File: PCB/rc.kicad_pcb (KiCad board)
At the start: 2 copper layers, 54.9 x 25.4 mm, 8 parts, among them J1 USB_C_Receptacle_USB2.0_16P, J2 USB_A, J3 OLED display, U1 ESP32-S3-WROOM-1U, U2 MAX3421EEHJ+T, U3 ME6211C33M5

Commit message: pcb update
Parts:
- added C3: C, Capacitor_SMD:C_0402_1005Metric_Pad0.74x0.62mm_HandSolder, B.Cu at (40.1, 69.1)
- added C4: C, Capacitor_SMD:C_0402_1005Metric_Pad0.74x0.62mm_HandSolder, B.Cu at (44.2, 71.9)
- added C5: C, Capacitor_SMD:C_0402_1005Metric_Pad0.74x0.62mm_HandSolder, B.Cu at (57.4, 63.2)
- added C7: C, Capacitor_SMD:C_0402_1005Metric_Pad0.74x0.62mm_HandSolder, B.Cu at (46.5, 71.4)
- added D1: ESD9B5.0ST5G, Diode_SMD:D_SOD-923, B.Cu at (48.0, 68.5)
- added D2: ESD9B5.0ST5G, Diode_SMD:D_SOD-923, B.Cu at (49.0, 68.5)
- added FB1: FerriteBead, Inductor_SMD:L_0603_1608Metric, B.Cu at (48.5, 70.8)
- added FB2: FerriteBead, Inductor_SMD:L_0603_1608Metric, B.Cu at (61.7, 66.0)
- added R1: R_US, Resistor_SMD:R_0402_1005Metric_Pad0.72x0.64mm_HandSolder, B.Cu at (50.0, 69.5)
- added R2: R_US, Resistor_SMD:R_0402_1005Metric_Pad0.72x0.64mm_HandSolder, B.Cu at (47.0, 69.1)
- added R3: R_US, Resistor_SMD:R_0402_1005Metric_Pad0.72x0.64mm_HandSolder, B.Cu at (50.5, 72.4)
- added REF**: MountingHole_2.2mm_M2_ISO7380_Pad_TopBottom, MountingHole:MountingHole_2.2mm_M2_ISO7380_Pad_TopBottom, F.Cu at (73.7, 53.3)
- added REF**: MountingHole_2.2mm_M2_ISO7380_Pad_TopBottom, MountingHole:MountingHole_2.2mm_M2_ISO7380_Pad_TopBottom, F.Cu at (31.1, 73.7)
- added REF**: MountingHole_2.2mm_M2_ISO7380_Pad_TopBottom, MountingHole:MountingHole_2.2mm_M2_ISO7380_Pad_TopBottom, F.Cu at (31.1, 53.3)
- added REF**: MountingHole_2.2mm_M2_ISO7380_Pad_TopBottom, MountingHole:MountingHole_2.2mm_M2_ISO7380_Pad_TopBottom, F.Cu at (73.7, 73.7)
- added Y1: Crystal, Crystal:Crystal_SMD_G8-2Pin_3.2x1.5mm, B.Cu at (42.7, 70.1)
- C1, C2, J1, U2, U3: moved to B.Cu
- J3: footprint Connector_PinSocket_1.27mm:PinSocket_1x07_P1.27mm_Vertical -> Connector_PinSocket_2.54mm:PinSocket_1x07_P2.54mm_Horizontal
- moved U2 24.8 mm to (47.2, 62.0), turned to -90 degrees
- moved C2 24.3 mm to (37.1, 65.4), turned to -90 degrees
- moved C1 22.5 mm to (39.0, 65.4), turned to -90 degrees
- moved U3 20.1 mm to (37.4, 61.2), turned to -90 degrees
- moved J3 11.4 mm to (44.7, 53.1), turned to 90 degrees
- moved J2 9.91 mm to (59.7, 63.1)
- moved J1 6.12 mm to (62.7, 72.7), turned to 180 degrees
- moved U1 4.90 mm to (43.7, 65.2)
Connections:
- C1 pad 1: Net-(J2-VBUS) -> Net-(U3-CE)
- J1 pad A4: Net-(J2-VBUS) -> Net-(U3-CE)
- J1 pad A9: Net-(J2-VBUS) -> Net-(U3-CE)
- J1 pad B4: Net-(J2-VBUS) -> Net-(U3-CE)
- J1 pad B9: Net-(J2-VBUS) -> Net-(U3-CE)
- J2 pad 2: unconnected-(J2-D--Pad2) -> Net-(J2-D-)
- J2 pad 3: unconnected-(J2-D+-Pad3) -> Net-(J2-D+)
- U1 pad 17: unconnected-(U1-IO9-Pad17) -> Net-(U1-IO9)
- U1 pad 3: unconnected-(U1-EN-Pad3) -> Net-(J3-Pin_2)
- U2 pad 18: unconnected-(U2-INT-Pad18) -> Net-(U1-IO9)
- U2 pad 2: unconnected-(U2-VL-Pad2) -> Net-(J3-Pin_2)
- U2 pad 20: unconnected-(U2-D--Pad20) -> Net-(D2-A1)
- U2 pad 21: unconnected-(U2-D+-Pad21) -> Net-(D1-A1)
- U2 pad 22: unconnected-(U2-VBCOMP-Pad22) -> Net-(U2-VBCOMP)
- U2 pad 24: unconnected-(U2-XI-Pad24) -> Net-(U2-XI)
- U2 pad 25: unconnected-(U2-XO-Pad25) -> Net-(U2-XO)
- U3 pad 1: Net-(J2-VBUS) -> Net-(U3-CE)
- U3 pad 3: Net-(J2-VBUS) -> Net-(U3-CE)
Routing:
- net Net-(U3-CE): track 0.00 -> 60.4 mm
- net Net-(U1-IO13): track 42.2 -> 5.86 mm, vias 0 -> 1
- net Net-(U1-IO10): track 46.3 -> 10.5 mm, vias 0 -> 1
- net Net-(J2-VBUS): track 34.6 -> 5.20 mm
- net Net-(J3-Pin_3): track 48.6 -> 19.5 mm, vias 0 -> 1
- net Net-(J2-D+): track 0.00 -> 25.6 mm
- net Net-(J2-D-): track 0.00 -> 18.9 mm
- net Net-(J3-Pin_6): track 27.6 -> 44.8 mm, vias 1 -> 0
- net Net-(J3-Pin_4): track 34.2 -> 17.3 mm
- net Net-(J1-SHIELD): track 34.9 -> 20.2 mm, vias 0 -> 6
- net Net-(U1-IO9): track 0.00 -> 11.5 mm, vias 0 -> 2
- net Net-(U2-XO): track 0.00 -> 10.5 mm
- net Net-(J3-Pin_5): track 20.7 -> 11.3 mm, vias 1 -> 0
- net Net-(U2-XI): track 0.00 -> 7.12 mm
- net Net-(J3-Pin_2): track 55.0 -> 49.1 mm, vias 2 -> 1
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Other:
- board size 54.9 x 25.4 mm -> 47.6 x 25.4 mm

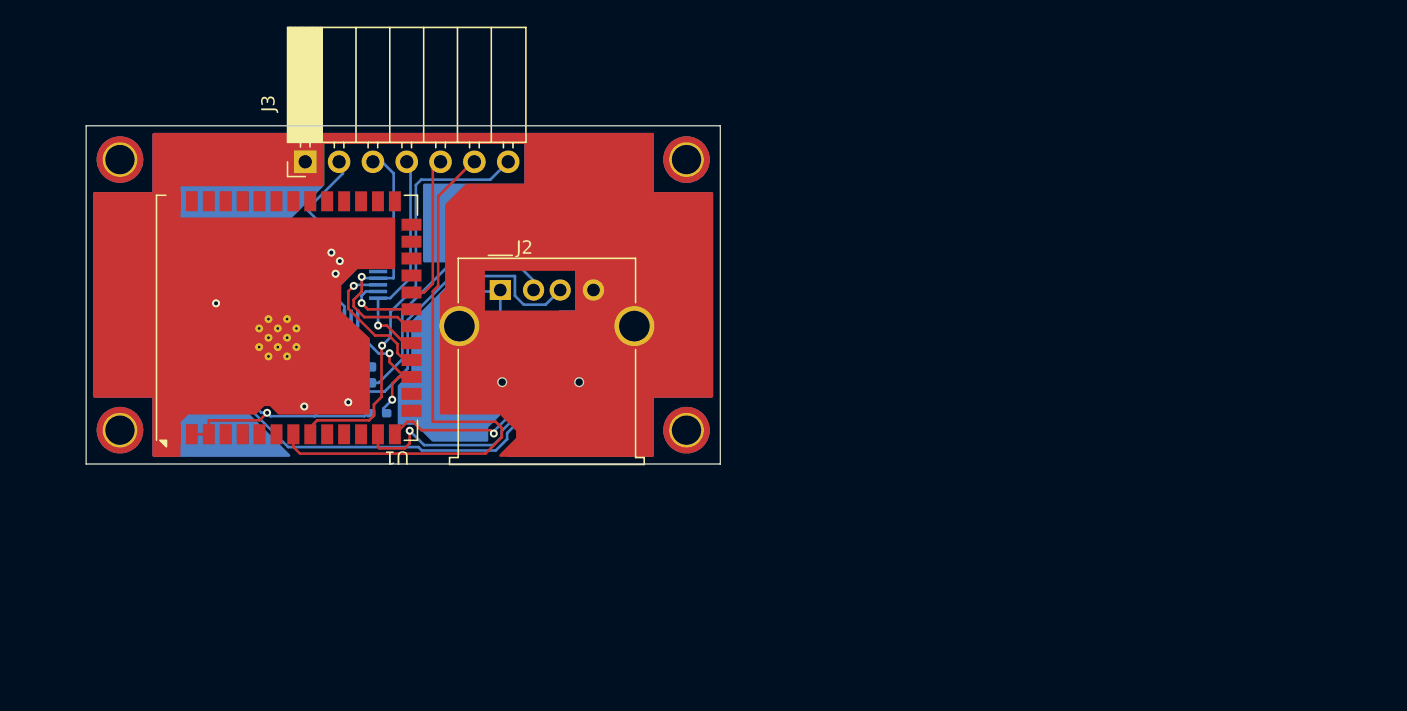
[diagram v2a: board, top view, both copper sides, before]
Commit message: 3 inch display
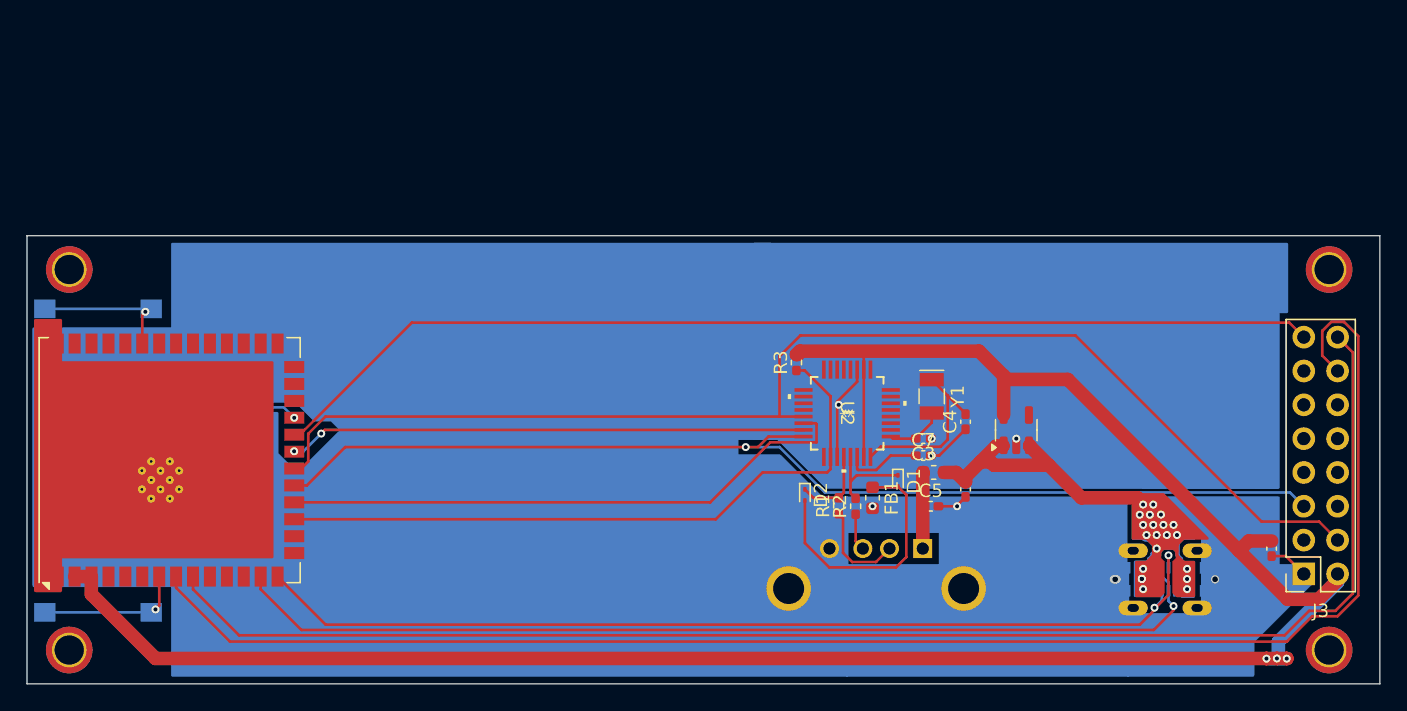
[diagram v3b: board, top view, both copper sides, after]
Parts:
- added SW1: SW_Omron_B3FS, Button_Switch_SMD:SW_SPST_Omron_B3FS-105xP, B.Cu at (29.5, 66.8)
- added SW2: SW_Omron_B3FS, Button_Switch_SMD:SW_SPST_Omron_B3FS-105xP, B.Cu at (29.5, 85.1)
- added SW3: SW_Omron_B3FS, Button_Switch_SMD:SW_SPST_Omron_B3FS-105xP, B.Cu at (29.2, 75.9)
- C1, C2, C3, C4, C5, C7, D1, D2, FB1, FB2, R1, R2, R3, U2, U3, Y1: moved to F.Cu
- J1: footprint Connector_USB:USB_C_Receptacle_GCT_USB4110 -> usbc:GCT_USB4120-03-C_REVA
- J2: footprint Connector_USB:USB_A_Molex_67643_Horizontal -> usb-a vertical:ONSHORE_USB-A1VSB6; moved to B.Cu
- J3: value OLED display -> Conn_02x08_Odd_Even; footprint Connector_PinSocket_2.54mm:PinSocket_1x07_P2.54mm_Horizontal -> Connector_PinSocket_2.54mm:PinSocket_2x08_P2.54mm_Vertical
- moved C2 82.3 mm to (117.6, 82.5)
- moved J3 81.6 mm to (120.0, 84.5), turned to 180 degrees
- moved U3 62.3 mm to (98.4, 73.7), turned to 90 degrees
- moved C1 57.1 mm to (94.6, 78.1)
- moved C3 51.6 mm to (91.4, 74.3), turned to 180 degrees
- moved REF** 51.0 mm to (121.9, 90.2)
- moved C4 50.4 mm to (94.6, 73.0), turned to 90 degrees
- moved Y1 49.4 mm to (92.1, 71.1), turned to -90 degrees
- moved REF** 49.0 mm to (121.9, 61.6)
- moved J1 48.5 mm to (109.6, 84.9)
- moved C7 45.2 mm to (91.4, 75.6), turned to 0 degrees
- moved D1 42.5 mm to (89.5, 77.5)
- moved R2 40.7 mm to (86.4, 79.4)
- moved FB1 39.9 mm to (87.6, 78.7)
- moved U2 39.9 mm to (85.7, 72.4)
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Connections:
- C1 pad 2: Net-(J1-SHIELD) -> /GND
- C2 pad 2: Net-(J1-SHIELD) -> /GND
- C3 pad 1: Net-(J1-SHIELD) -> /GND
- C4 pad 1: Net-(J1-SHIELD) -> /GND
- C5 pad 2: Net-(J1-SHIELD) -> /GND
- C7 pad 2: Net-(J1-SHIELD) -> /GND
- FB1 pad 2: Net-(J1-SHIELD) -> /GND
- J1 pad A1: Net-(J1-SHIELD) -> /GND
- J1 pad A12: Net-(J1-SHIELD) -> /GND
- J1 pad B1: Net-(J1-SHIELD) -> /GND
- J1 pad B12: Net-(J1-SHIELD) -> /GND
- J1 pad S1: Net-(J1-SHIELD) -> /GND
- J2 pad 4: Net-(J1-SHIELD) -> /GND
- J3 pad 1: Net-(J1-SHIELD) -> /GND
- J3 pad 3: Net-(J3-Pin_3) -> unconnected-(J3-Pin_3-Pad3)
- J3 pad 4: Net-(J3-Pin_4) -> /CLK
- J3 pad 5: Net-(J3-Pin_5) -> /MOSI
- J3 pad 6: Net-(J3-Pin_6) -> unconnected-(J3-Pin_6-Pad6)
- J3 pad 7: Net-(J3-Pin_7) -> unconnected-(J3-Pin_7-Pad7)
- U1 pad 1: Net-(J1-SHIELD) -> /GND
- U1 pad 19: Net-(J3-Pin_4) -> /MOSI
- U1 pad 20: Net-(J3-Pin_3) -> /CLK
- U1 pad 22: Net-(J3-Pin_5) -> /RES
- U1 pad 23: unconnected-(U1-IO21-Pad23) -> Net-(U1-IO21)
- U1 pad 35: unconnected-(U1-IO42-Pad35) -> Net-(U1-IO42)
- U1 pad 40: Net-(J1-SHIELD) -> /GND
- U1 pad 41: Net-(J1-SHIELD) -> /GND
- U1 pad 7: unconnected-(U1-IO7-Pad7) -> Net-(U1-IO7)
- U1 pad 8: Net-(J3-Pin_6) -> /DC
- U1 pad 9: Net-(J3-Pin_7) -> /CS
- U2 pad 13: Net-(J3-Pin_3) -> /CLK
- U2 pad 16: Net-(J3-Pin_4) -> /MOSI
- U2 pad 19: Net-(J1-SHIELD) -> /GND
- U2 pad 3: Net-(J1-SHIELD) -> /GND
- U3 pad 2: Net-(J1-SHIELD) -> /GND
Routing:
- net /GND: track 0.00 -> 131.6 mm, vias 0 -> 6
- net /DC: track 0.00 -> 119.1 mm
- net Net-(J3-Pin_2): track 49.1 -> 168.2 mm, vias 1 -> 3
- net /CS: track 0.00 -> 110.5 mm
- net /CLK: track 0.00 -> 94.5 mm
- net /MOSI: track 0.00 -> 83.5 mm, vias 0 -> 1
- net /RES: track 0.00 -> 79.8 mm
- net Net-(U1-IO20): track 16.7 -> 74.8 mm, vias 1 -> 2
- net Net-(U1-IO19): track 20.8 -> 74.9 mm
- net Net-(J3-Pin_6): track 44.8 -> 0.00 mm
- net Net-(U1-IO9): track 11.5 -> 50.7 mm, vias 2 -> 0
- net Net-(U1-IO13): track 5.86 -> 38.9 mm, vias 1 -> 2
- net Net-(U1-IO10): track 10.5 -> 43.5 mm, vias 1 -> 0
- net Net-(J3-Pin_7): track 31.9 -> 0.00 mm, vias 1 -> 0
- net Net-(J2-D+): track 25.6 -> 2.80 mm
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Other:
- board size 47.6 x 25.4 mm -> 101.6 x 33.7 mm

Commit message: more board
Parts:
- removed D1, D2: ESD9B5.0ST5G, Diode_SMD:D_SOD-923
- removed REF** (x4): MountingHole_2.2mm_M2_ISO7380_Pad_TopBottom, MountingHole:MountingHole_2.2mm_M2_ISO7380_Pad_TopBottom
- added C6: 100nf, Capacitor_SMD:C_0402_1005Metric_Pad0.74x0.62mm_HandSolder, F.Cu at (116.3, 82.5)
- added D3: PGB1010603MR, esd:DIOC1608X36N, F.Cu at (89.7, 78.7)
- added D4: PGB1010603MR, esd:DIOC1608X36N, F.Cu at (81.3, 78.7)
- added R4: 5.1k, Resistor_SMD:R_0402_1005Metric_Pad0.72x0.64mm_HandSolder, B.Cu at (111.3, 81.3)
- added R5: 5.1k, Resistor_SMD:R_0402_1005Metric_Pad0.72x0.64mm_HandSolder, B.Cu at (108.2, 88.4)
- C1, C2: value C -> 10mfd
- C3, C4: value C -> 22pf
- R1, R2: value R_US -> 22
- R3: value R_US -> 10k
- Y1: value Crystal -> 12Mhz/12pf; footprint Crystal:Crystal_SMD_G8-2Pin_3.2x1.5mm -> Crystal:Crystal_SMD_HC49-SD
- moved Y1 4.85 mm to (96.8, 69.9)
- moved U3 2.79 mm to (101.2, 73.7)
- moved C4 2.74 mm to (91.9, 72.4)
- moved C1 0.13 mm to (94.7, 78.1)
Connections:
- J1 pad A5: unconnected-(J1-CC1-PadA5) -> Net-(J1-CC1)
- J1 pad B5: unconnected-(J1-CC2-PadB5) -> Net-(J1-CC2)
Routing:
- net Net-(J3-Pin_2): track 168.2 -> 181.0 mm
- net /GND: track 131.6 -> 123.4 mm, vias 6 -> 8
- net Net-(U2-XI): track 13.3 -> 20.7 mm
- net Net-(U3-CE): track 46.4 -> 41.1 mm, vias 21 -> 18
- net /CLK: track 94.5 -> 99.5 mm
- net /RES: track 79.8 -> 84.2 mm
- net Net-(U2-XO): track 4.36 -> 8.41 mm
- net Net-(J1-CC2): track 0.00 -> 3.63 mm
- net Net-(J1-CC1): track 0.00 -> 2.84 mm
- net Net-(U2-D-): track 6.03 -> 7.36 mm
- net Net-(U1-IO20): track 74.8 -> 75.9 mm
- net Net-(U2-D+): track 7.00 -> 8.00 mm
- net Net-(D3-Pad2): track 19.4 -> 18.5 mm
- net Net-(U1-IO19): track 74.9 -> 75.8 mm
